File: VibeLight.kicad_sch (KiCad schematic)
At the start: 14 parts, among them SW1 SW_Push, SW2 SW_Push

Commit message: completed rev1 of PCB layout
need to double check components and other elements, connections, and add values
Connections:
- net MCU/SCL: now also R3.2
- net MCU/SDA: now also R4.2
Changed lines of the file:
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@@
 (kicad_sch (version 20230121) (generator eeschema)
   (paper "A4")
-  (junction (at 142.24 80.01) (diameter 0) (color 0 0 0 0)
-  )
   (junction (at 30.48 106.68) (diameter 0) (color 0 0 0 0)
   )
@@
   (junction (at 212.09 49.53) (diameter 0) (color 0 0 0 0)
   )
+  (junction (at 138.43 73.66) (diameter 0) (color 0 0 0 0)
+  )
   (junction (at 27.94 107.95) (diameter 0) (color 0 0 0 0)
   )
@@
     (stroke (width 0) (type default))
   )
-  (bus (pts (xy 142.24 80.01) (xy 152.4 80.01))
-    (stroke (width 0) (type default))
-  )
-  (bus (pts (xy 124.46 74.93) (xy 124.46 80.01))
+  (bus (pts (xy 124.46 77.47) (xy 124.46 80.01))
     (stroke (width 0) (type default))
   )
@@
     (stroke (width 0) (type default))
   )
-  (bus (pts (xy 137.16 80.01) (xy 142.24 80.01))
+  (bus (pts (xy 137.16 80.01) (xy 152.4 80.01))
     (stroke (width 0) (type default))
   )
@@
     (stroke (width 0) (type default))
   )
+  (wire (pts (xy 137.16 90.17) (xy 137.16 93.98))
+    (stroke (width 0) (type default))
+  )
   (bus (pts (xy 92.71 72.39) (xy 120.65 72.39))
     (stroke (width 0) (type default))
@@
     (stroke (width 0) (type default))
   )
+  (bus (pts (xy 142.24 93.98) (xy 142.24 76.2))
+    (stroke (width 0) (type default))
+  )
   (wire (pts (xy 27.94 106.68) (xy 30.48 106.68))
     (stroke (width 0) (type default))
@@
     (stroke (width 0) (type default))
   )
+  (wire (pts (xy 142.24 85.09) (xy 142.24 93.98))
+    (stroke (width 0) (type default))
+  )
   (wire (pts (xy 227.33 124.46) (xy 166.37 124.46))
     (stroke (width 0) (type default))
@@
     (stroke (width 0) (type default))
   )
-  (bus (pts (xy 120.65 73.66) (xy 142.24 73.66))
+  (bus (pts (xy 120.65 73.66) (xy 138.43 73.66))
     (stroke (width 0) (type default))
   )
@@
     (stroke (width 0) (type default))
   )
-  (bus (pts (xy 156.21 74.93) (xy 124.46 74.93))
+  (bus (pts (xy 156.21 77.47) (xy 124.46 77.47))
     (stroke (width 0) (type default))
   )
@@
     (stroke (width 0) (type default))
   )
-  (bus (pts (xy 142.24 77.47) (xy 156.21 77.47))
+  (bus (pts (xy 142.24 74.93) (xy 156.21 74.93))
     (stroke (width 0) (type default))
   )
@@
     (stroke (width 0) (type default))
   )
+  (bus (pts (xy 142.24 76.2) (xy 138.43 76.2))
+    (stroke (width 0) (type default))
+  )
   (wire (pts (xy 133.35 85.09) (xy 142.24 85.09))
     (stroke (width 0) (type default))
@@
     (stroke (width 0) (type default))
   )
+  (bus (pts (xy 138.43 73.66) (xy 142.24 73.66))
+    (stroke (width 0) (type default))
+  )
   (bus (pts (xy 87.63 80.01) (xy 124.46 80.01))
     (stroke (width 0) (type default))
@@
     (stroke (width 0) (type default))
   )
-  (bus (pts (xy 142.24 80.01) (xy 142.24 93.98))
+  (bus (pts (xy 138.43 73.66) (xy 138.43 76.2))
     (stroke (width 0) (type default))
   )
@@
     (stroke (width 0) (type default))
   )
-  (bus (pts (xy 142.24 77.47) (xy 142.24 73.66))
-    (stroke (width 0) (type default))
-  )
+  (bus (pts (xy 142.24 74.93) (xy 142.24 73.66))
+    (stroke (width 0) (type default))
+  )

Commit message: Changes from DR call
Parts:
- removed R5: R, Resistor_SMD:R_0603_1608Metric_Pad0.98x0.95mm_HandSolder, symbol Device:R
- R3, R4: value R -> 4.7K
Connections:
- net BATT+: now also OUT_PINS1.1 (Pin_1)
- net GND: now also Accel1.12 (SDO/ADDR), SW1.2, SW2.2
- net +3V3: now reaches Accel1.1 (Vdd_I/O)
- net +3V3: now also Accel1.6 (Vs), Accel1.7 (~{CS}), C4.1, Light1.1 (VDD), PWR_REG1.4 (OUT), R3.1, R4.1, RV2.1, Temp1.3 (VDD)
- removed net Audio Input/PWR: Accel1.6 (Vs), Accel1.7 (~{CS}), C4.1, Light1.1 (VDD), OUT_PINS1.1 (Pin_1), PWR_REG1.4 (OUT), R3.1, R4.1, RV2.1, SW1.2, SW2.2, Temp1.3 (VDD)

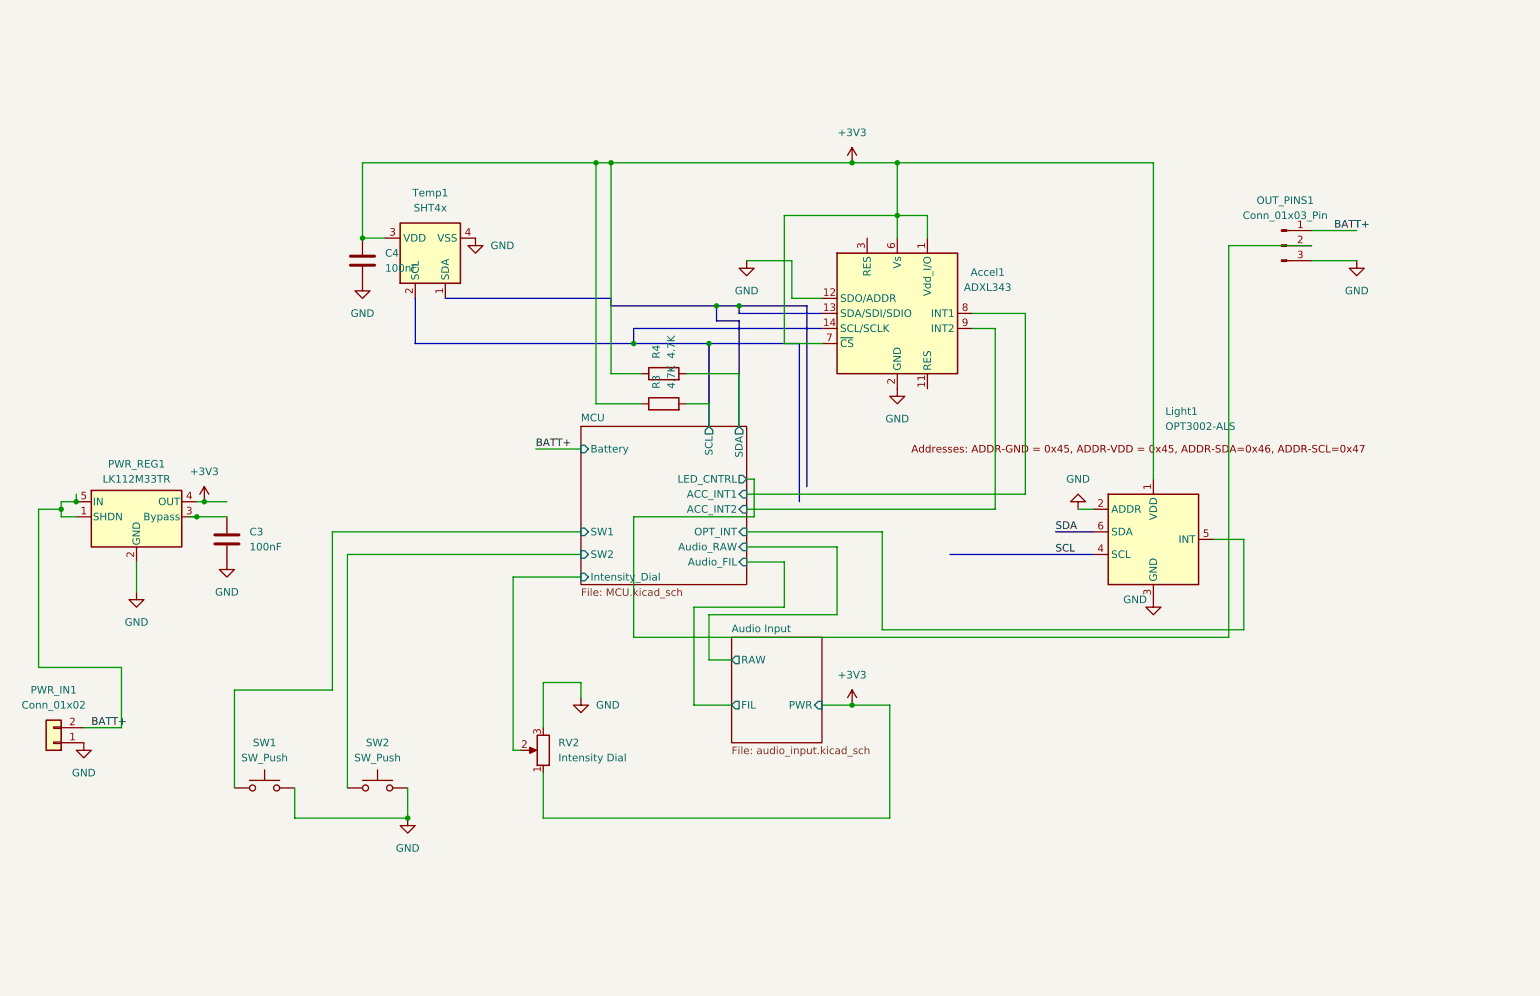
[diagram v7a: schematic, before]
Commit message: pcB rev2
need to fix reference texts on PCB, figure out MEMs mic wiring
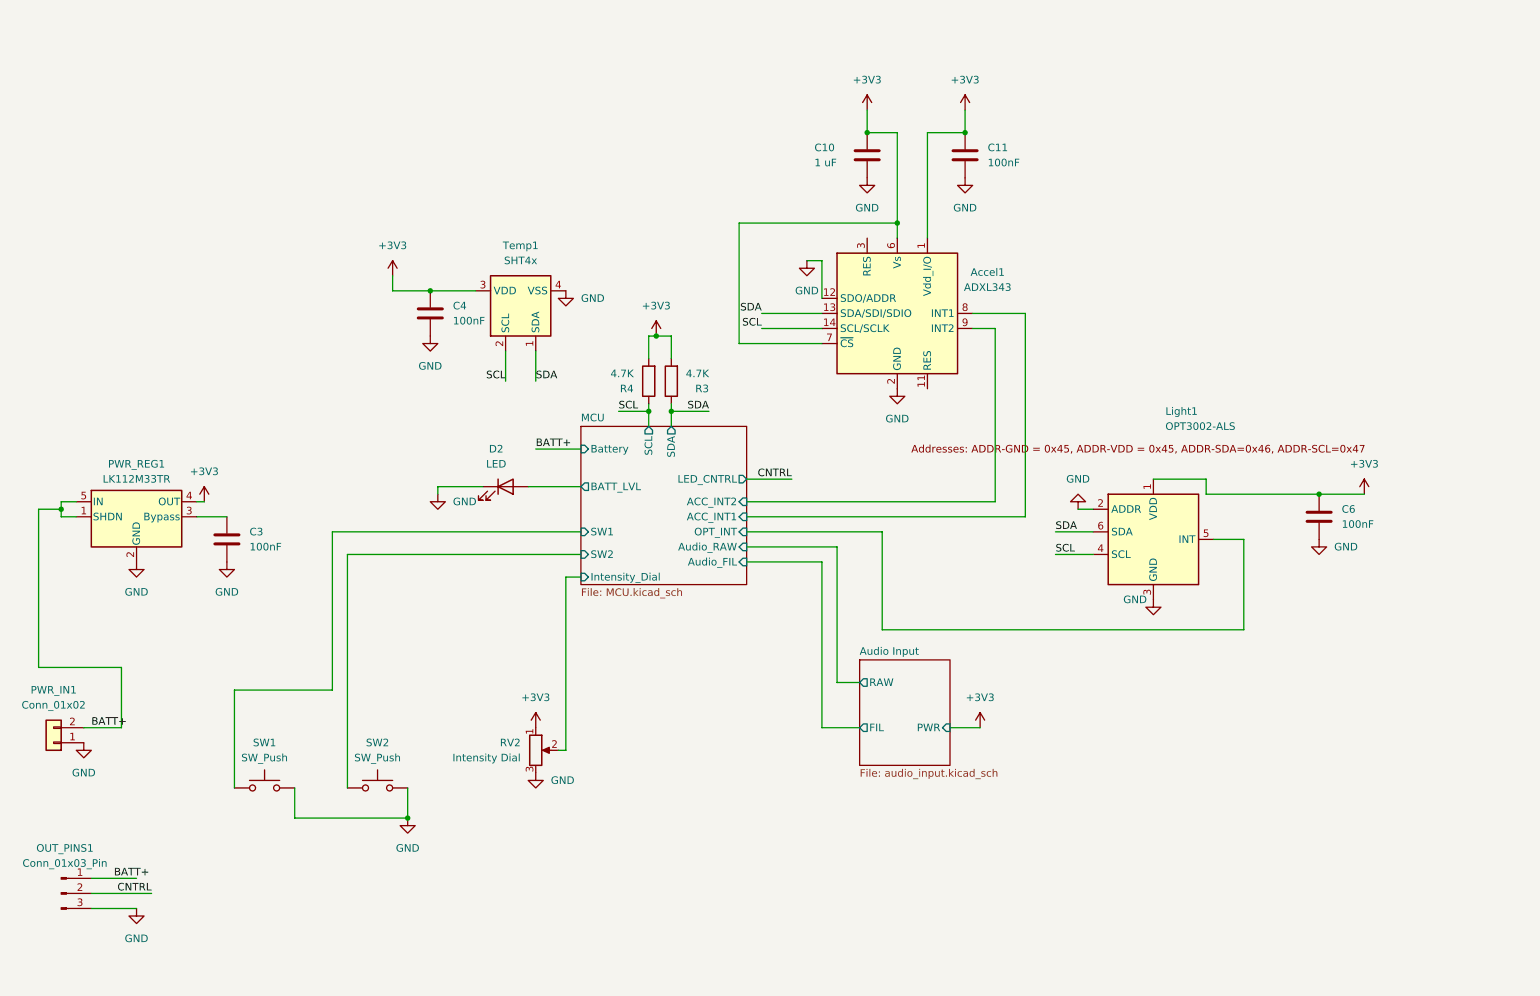
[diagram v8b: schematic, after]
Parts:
- added C10: 1 uF, Capacitor_SMD:C_0603_1608Metric_Pad1.08x0.95mm_HandSolder, symbol Device:C
- added C11, C6: 100nF, Capacitor_SMD:C_0603_1608Metric_Pad1.08x0.95mm_HandSolder, symbol Device:C
- added D2: LED, LED_SMD:LED_0603_1608Metric_Pad1.05x0.95mm_HandSolder, symbol Device:LED
- OUT_PINS1: footprint Connector_JST:JST_GH_BM03B-GHS-TBT_1x03-1MP_P1.25mm_Vertical -> Connector_JST:JST_GH_SM03B-GHS-TB_1x03-1MP_P1.25mm_Horizontal
- PWR_IN1: footprint Connector_JST:JST_GH_BM02B-GHS-TBT_1x02-1MP_P1.25mm_Vertical -> Connector_JST:JST_GH_SM02B-GHS-TB_1x02-1MP_P1.25mm_Horizontal
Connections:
- net MCU/SCL is gone; now on net +3V3: R3.2
- net MCU/SDA is gone; now on net +3V3: R4.2
- net +3V3: now also C10.1, C11.1, C6.1; no longer R3.1, R4.1
- net GND: now also C10.2, C11.2, C6.2, D2.1 (K)
- net SCL: now also Accel1.14 (SCL/SCLK), Light1.4 (SCL), R4.1, Temp1.2 (SCL)
- net SDA: now also Accel1.13 (SDA/SDI/SDIO), Light1.6 (SDA), R3.1, Temp1.1 (SDA)
- net MCU/LED_CNTRL renamed CNTRL
- new net MCU/BATT_LVL: D2.2 (A)
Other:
- sheet MCU ports: added BATT_LVL; removed none
- moved on the sheet: C4, OUT_PINS1, R3, R4, RV2, Temp1
